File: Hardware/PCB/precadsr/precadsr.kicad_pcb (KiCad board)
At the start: 2 copper layers, 114 x 180 mm, 82 parts, among them J1 Synth_power_2x5, J10 Conn_01x10, J11 Conn_01x04, J12 2_pin_Molex_connector, J2 AudioJack2_SwitchT, J3 AudioJack2, J4 AudioJack2, J5 AudioJack2, J6 Conn_01x07, J7 2_pin_Molex_header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

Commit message: Final tweaks before fabbing; Kosmo_panel lib update
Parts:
- U1: footprint Package_DIP:DIP-8_W7.62mm -> ao_tht:DIP-8_W7.62mm_Socket_LongPads
- U3: value TL072 -> TL071
- moved C9 18.0 mm to (116.8, 101.6)
- moved C8 18.0 mm to (111.8, 119.4)
- moved U3 10.8 mm to (106.7, 106.7), turned to 270 degrees
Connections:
- U3 pad 2: Net-(U3-Pad1) -> THR
- U3 pad 3: GND -> Net-(R17-Pad1)
- U3 pad 5: Net-(R17-Pad1) -> Net-(U3-Pad5)
- U3 pad 6: THR -> LOOP_CONN_1
- U3 pad 7: LOOP_CONN_1 -> +12V
- U3 pad 8: +12V -> Net-(U3-Pad8)
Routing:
- net Net-(R17-Pad1): track 30.2 -> 21.3 mm
- net -12V: track 51.3 -> 59.4 mm
- net +12V: track 200.3 -> 196.3 mm
- net LOOP_CONN_1: track 119.6 -> 123.0 mm
- net Net-(U3-Pad1): track 2.54 -> 0.00 mm
- net DEC1: track 139.8 -> 138.0 mm
- net Net-(D4-Pad2): track 18.1 -> 17.6 mm
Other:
- board text added: "Caps socket (optional)"

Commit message: github url
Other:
- board text added: "Circuit design by Kassutronics Mods and PCB by Rich Holmes April 2021 https://github.com/holmesrichards/precadsr"
- board text removed: "Circuit design by Kassutronics Mods and PCB by Rich Holmes April 2021"

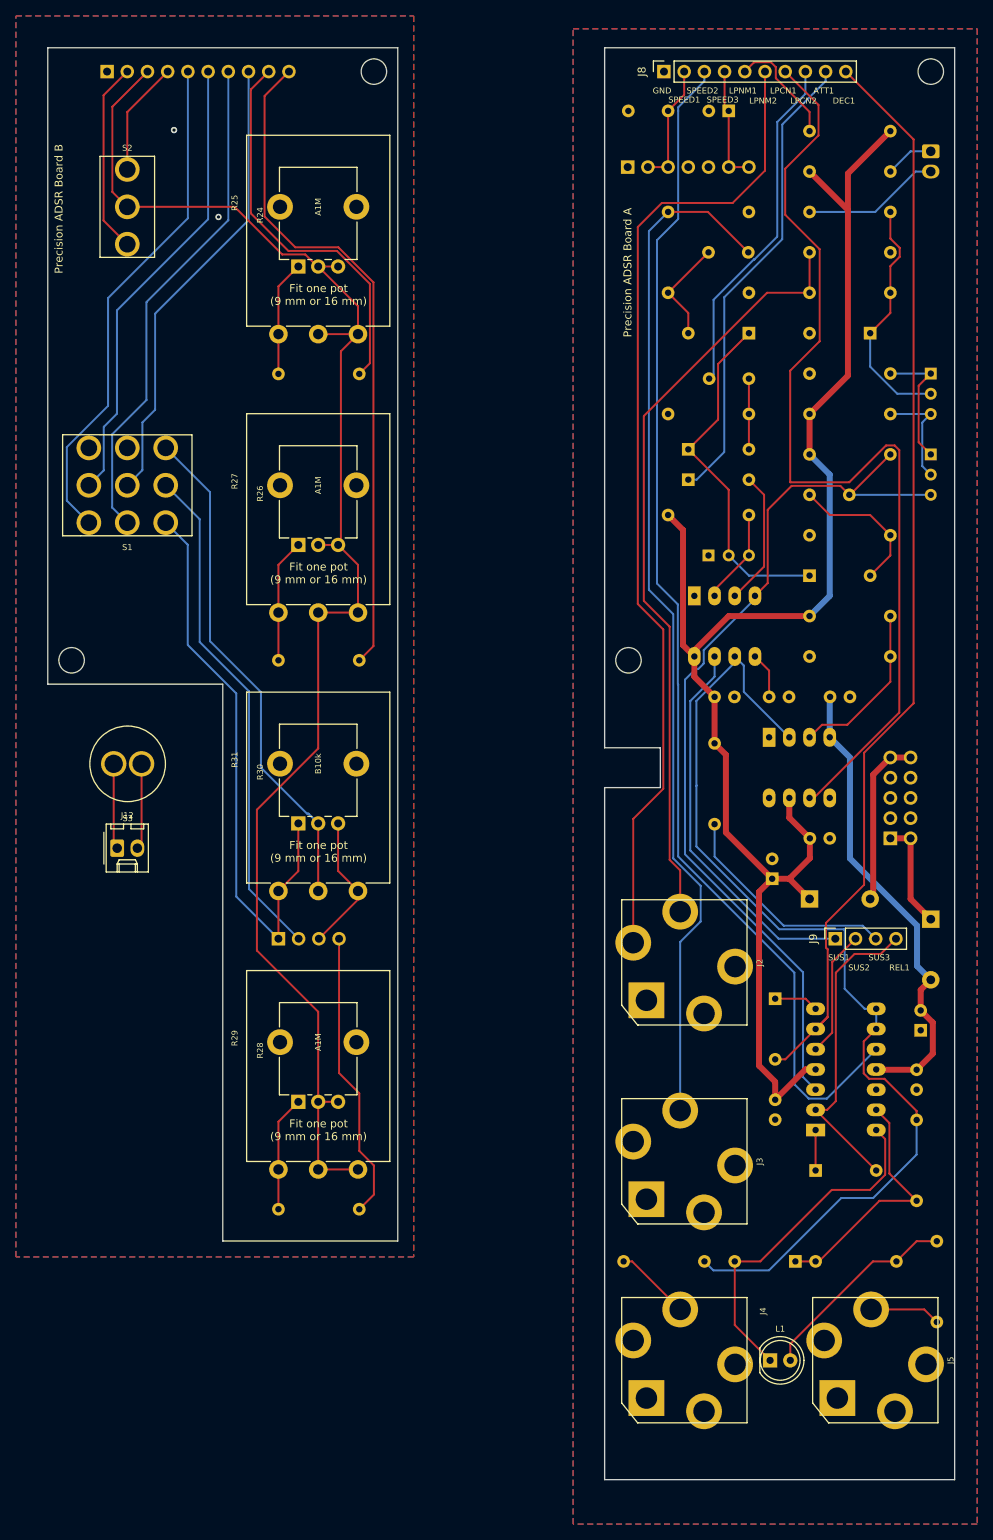
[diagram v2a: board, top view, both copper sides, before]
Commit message: Documentation, some cosmetic sh/PCB updates
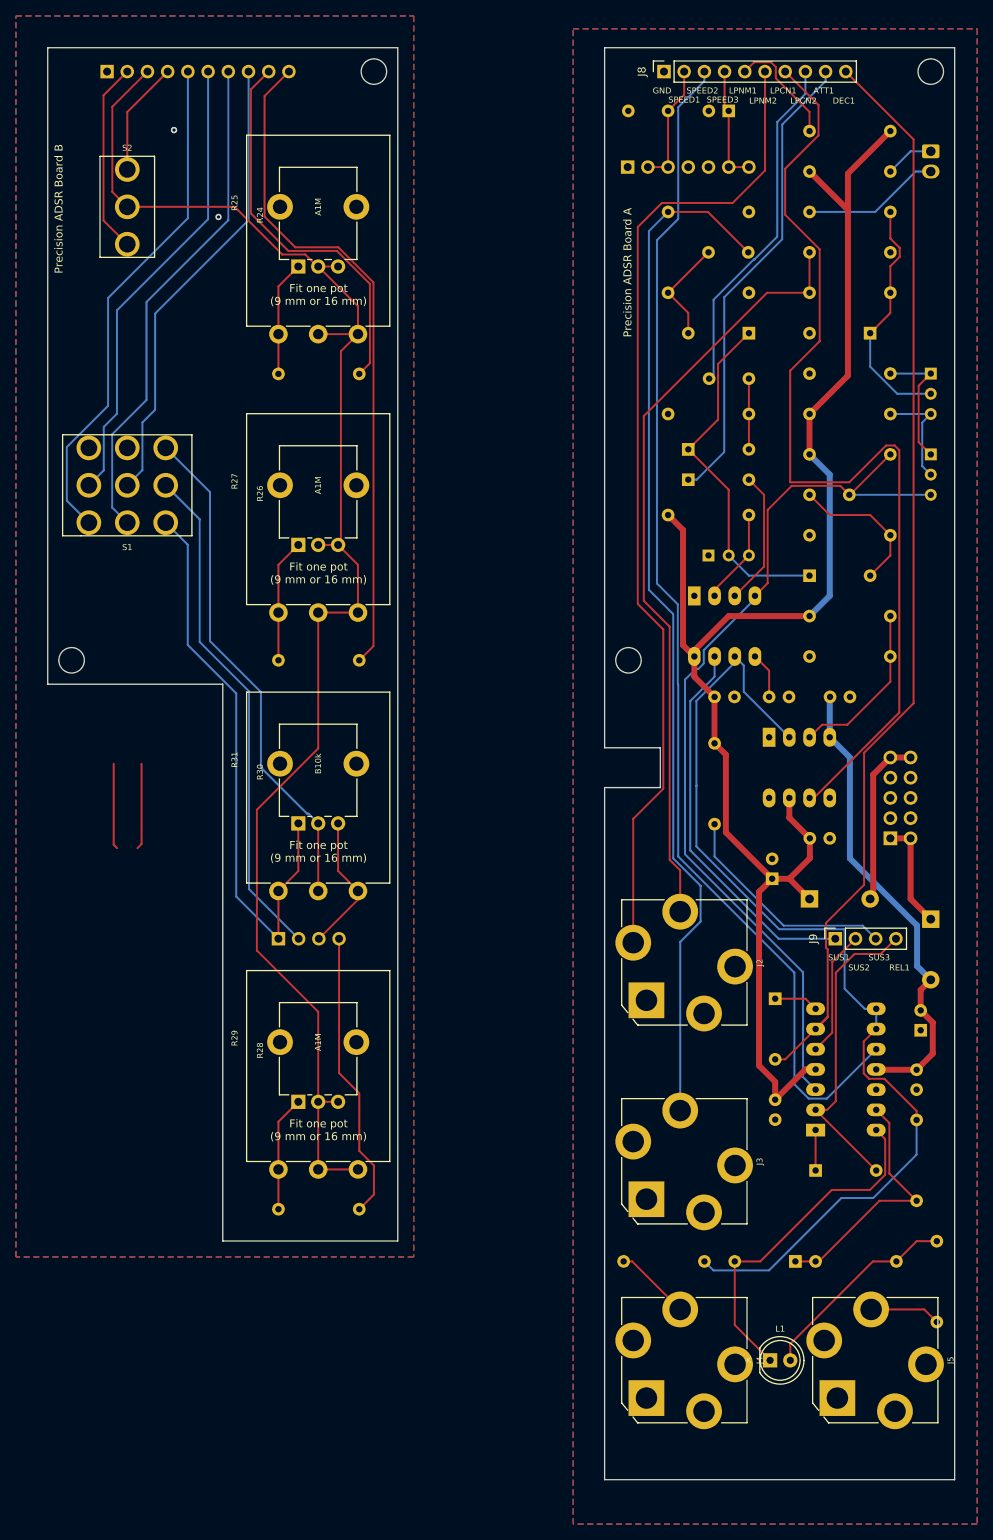
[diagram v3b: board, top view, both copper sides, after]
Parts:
- removed J12: 2_pin_Molex_connector, ao_tht:Molex_KK-254_AE-6410-02A_1x02_P2.54mm_Vertical
- removed S3: SW_Push, ao_tht:Push_button_A-5050
